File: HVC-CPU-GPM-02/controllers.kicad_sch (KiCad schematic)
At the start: 40 parts, among them P2 EXPANSION, P4 CONTROLLER 1, P5 CONTROLLER 2, U7 74LS368, U8 74LS368

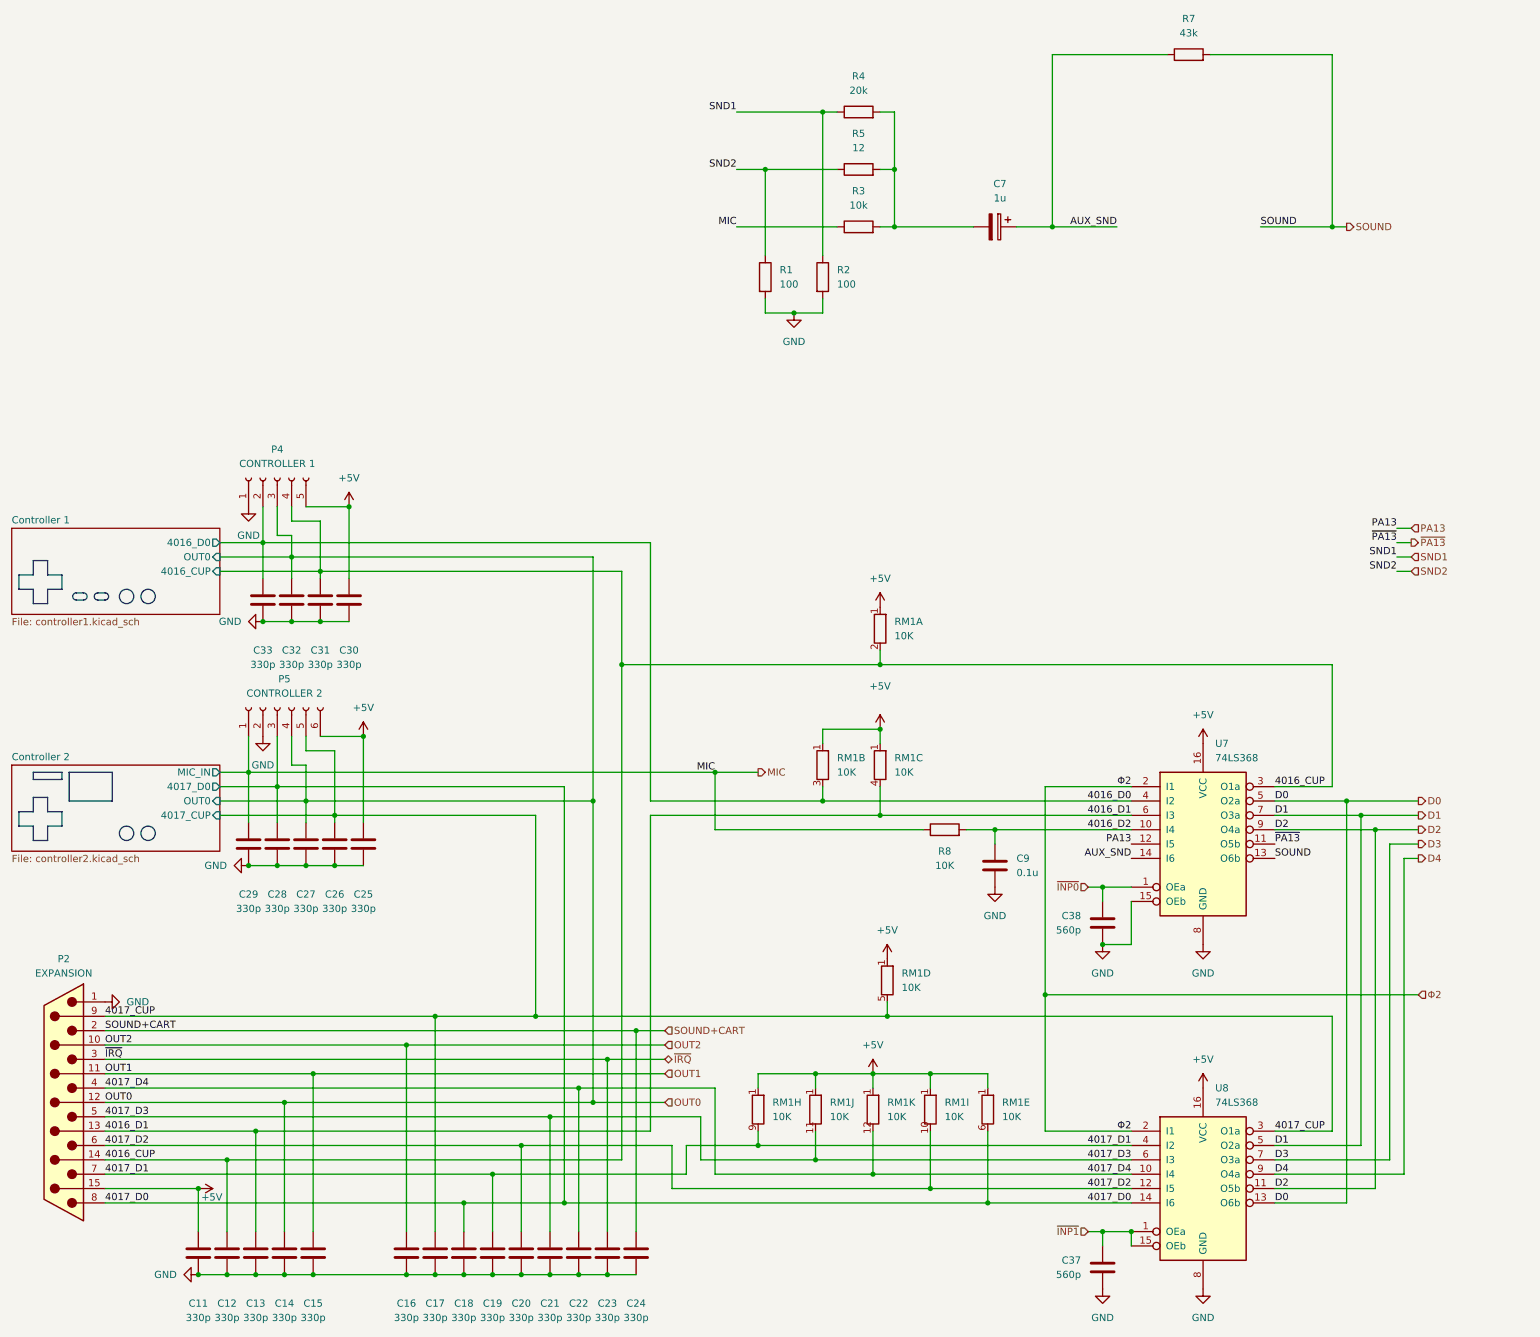
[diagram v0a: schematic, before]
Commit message: Refactor schematic: * Move audio and video circuits to dedicated sheet * Move power and mechanical to dedicated sheet Modify P1 Cart Connector symbol to: * split out audio ports * organize pins for easier wiring Modify 74LS346 symbol: * Split A/B ports to allow moving functions to related circuits Modify X1 crystal footprint: * change from stock footprint to custom footprint Correct crystal name from Y1 to X1
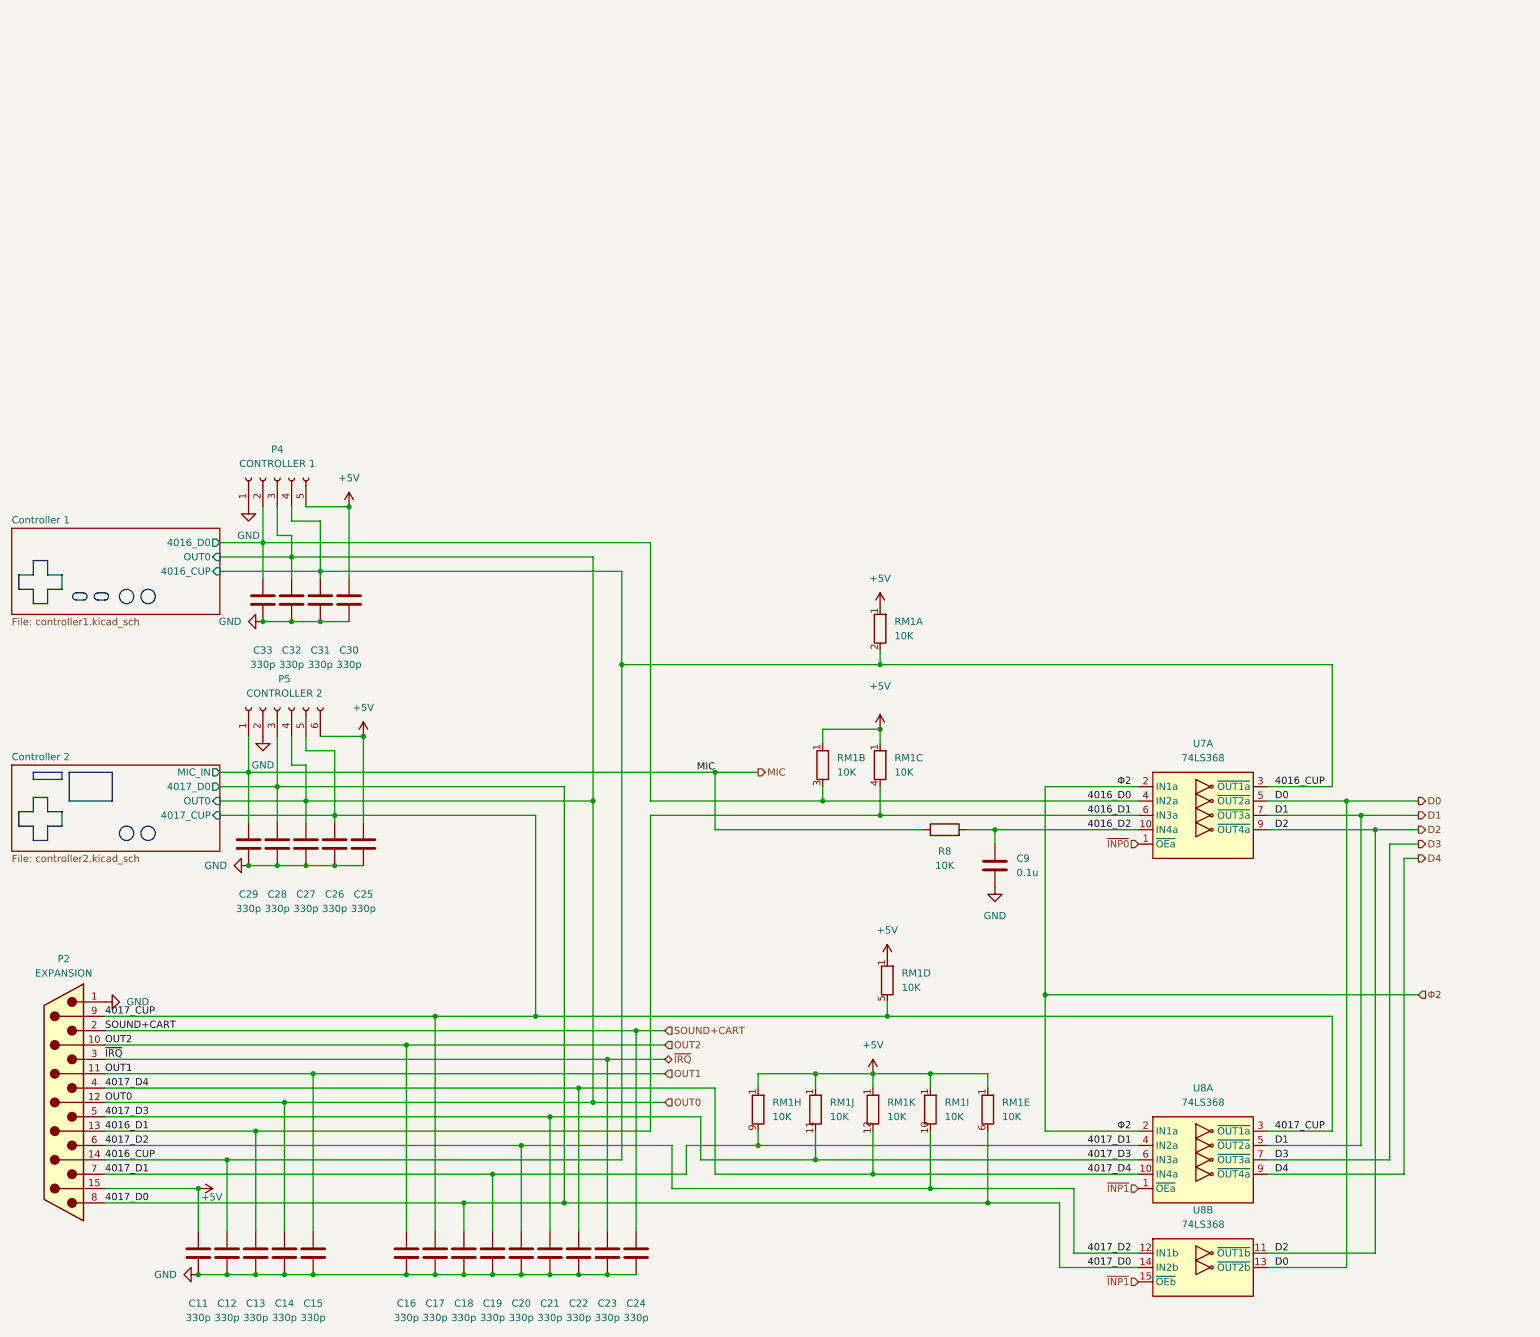
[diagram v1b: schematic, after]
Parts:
- removed C37, C38: 560p, Nintendo:C_Disc_D3.0mm_W2.0mm_P3.0mm, symbol Device:C
- removed C7: 1u, Capacitor_THT:CP_Radial_D5.0mm_P2.50mm, symbol Device:C_Polarized
- removed R1, R2: 100, Resistor_THT:R_Axial_DIN0207_L6.3mm_D2.5mm_P10.16mm_Horizontal, symbol Device:R
- removed R3: 10k, Resistor_THT:R_Axial_DIN0207_L6.3mm_D2.5mm_P10.16mm_Horizontal, symbol Device:R
- removed R4: 20k, Resistor_THT:R_Axial_DIN0207_L6.3mm_D2.5mm_P10.16mm_Horizontal, symbol Device:R
- removed R5: 12, Resistor_THT:R_Axial_DIN0207_L6.3mm_D2.5mm_P10.16mm_Horizontal, symbol Device:R
- removed R7: 43k, Resistor_THT:R_Axial_DIN0207_L6.3mm_D2.5mm_P10.16mm_Horizontal, symbol Device:R
- removed U8: 74LS368, Package_DIP:DIP-16_W7.62mm, symbol 74xx:74LS368
- added U8: 74LS368, Package_DIP:DIP-16_W7.62mm, symbol Famicom:74LS368
- U7: symbol 74xx:74LS368 -> Famicom:74LS368
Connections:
- net +5V: no longer U7.16 (VCC)
- net 4017_CUP: now also U8.3 (~{OUT1a})
- net 4017_D0: now also U8.14 (IN2b)
- net 4017_D1: now also U8.4 (IN2a)
- net 4017_D2: now also U8.12 (IN1b)
- net 4017_D3: now also U8.6 (IN3a)
- net 4017_D4: now also U8.10 (IN4a)
- net D0: now also U8.13 (~{OUT2b})
- net D1: now also U8.5 (~{OUT2a})
- net D2: now also U8.11 (~{OUT1b})
- net D3: now also U8.7 (~{OUT3a})
- net D4: now also U8.9 (~{OUT4a})
- net GND: no longer U7.15 (OEb), U7.8 (GND)
- net ~{INP1}: now also U8.1 (~{OEa}), U8.15 (~{OEb})
- net Φ2: now also U8.2 (IN1a)
- removed net AUX_SND: U7.14 (I6)
- removed net PA13: U7.12 (I5)
- removed net SOUND: U7.13 (O6b)
- removed net ~{PA13}: U7.11 (O5b)

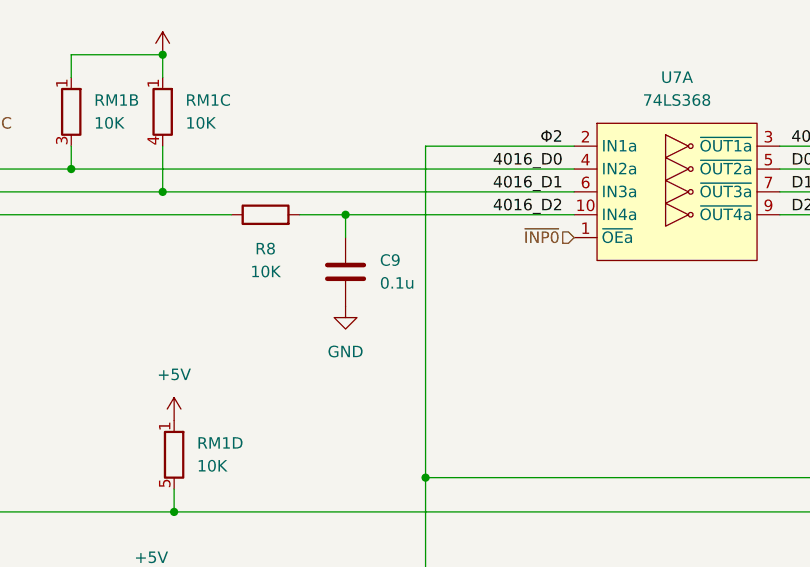
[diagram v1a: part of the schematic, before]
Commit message: Change symbols to functional layout instead of pin map layout Add technical page to store pinouts Organize and compact root page
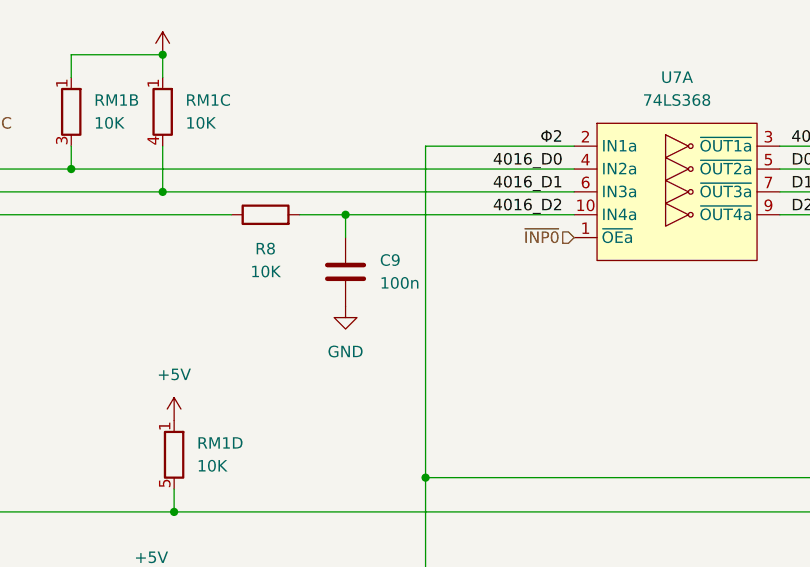
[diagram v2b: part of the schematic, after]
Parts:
- C9: value 0.1u -> 100n
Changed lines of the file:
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@@
 			)
 		)
-		(property "Value" "0.1u"
+		(property "Value" "100n"
 			(at 194.31 88.8999 0)
 			(effects

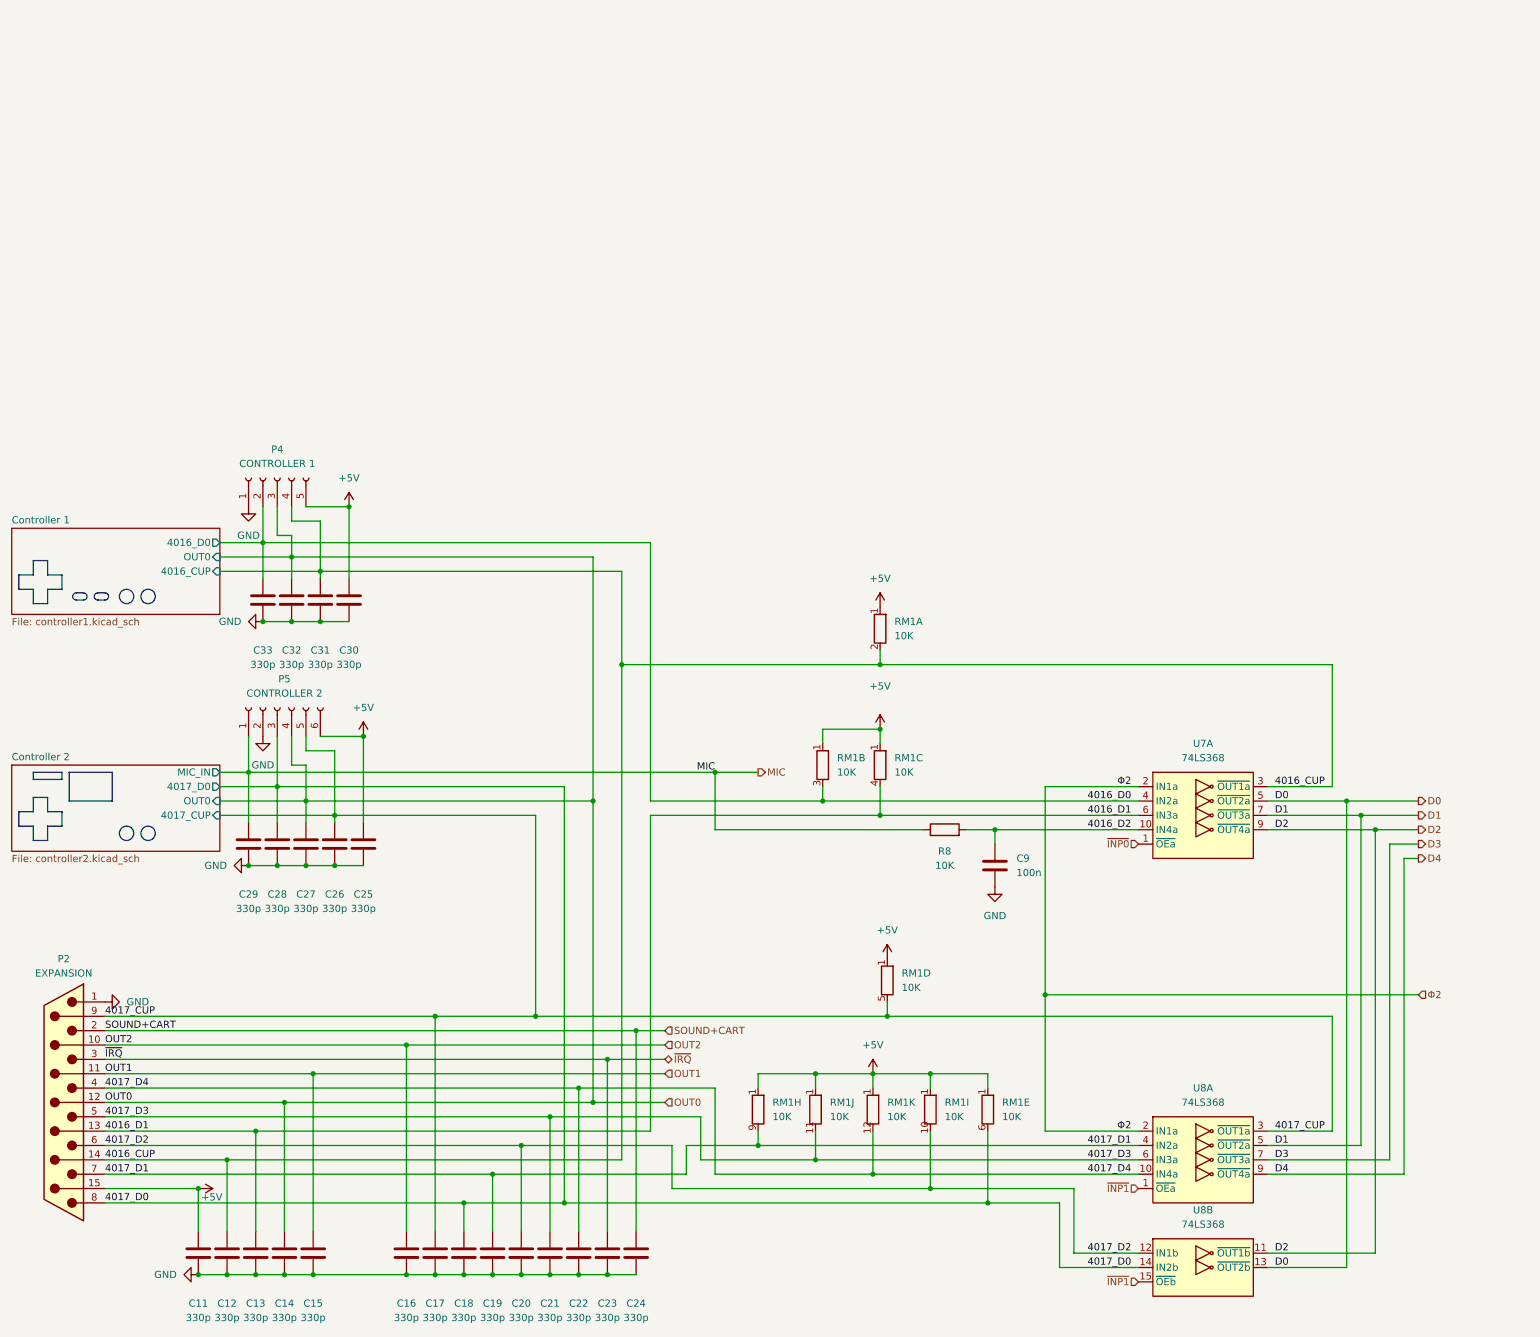
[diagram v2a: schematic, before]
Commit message: Rearranged pins on some symbols to simplify schematic wiring Removed schematics for controller PCBs Added PNG version of schematics
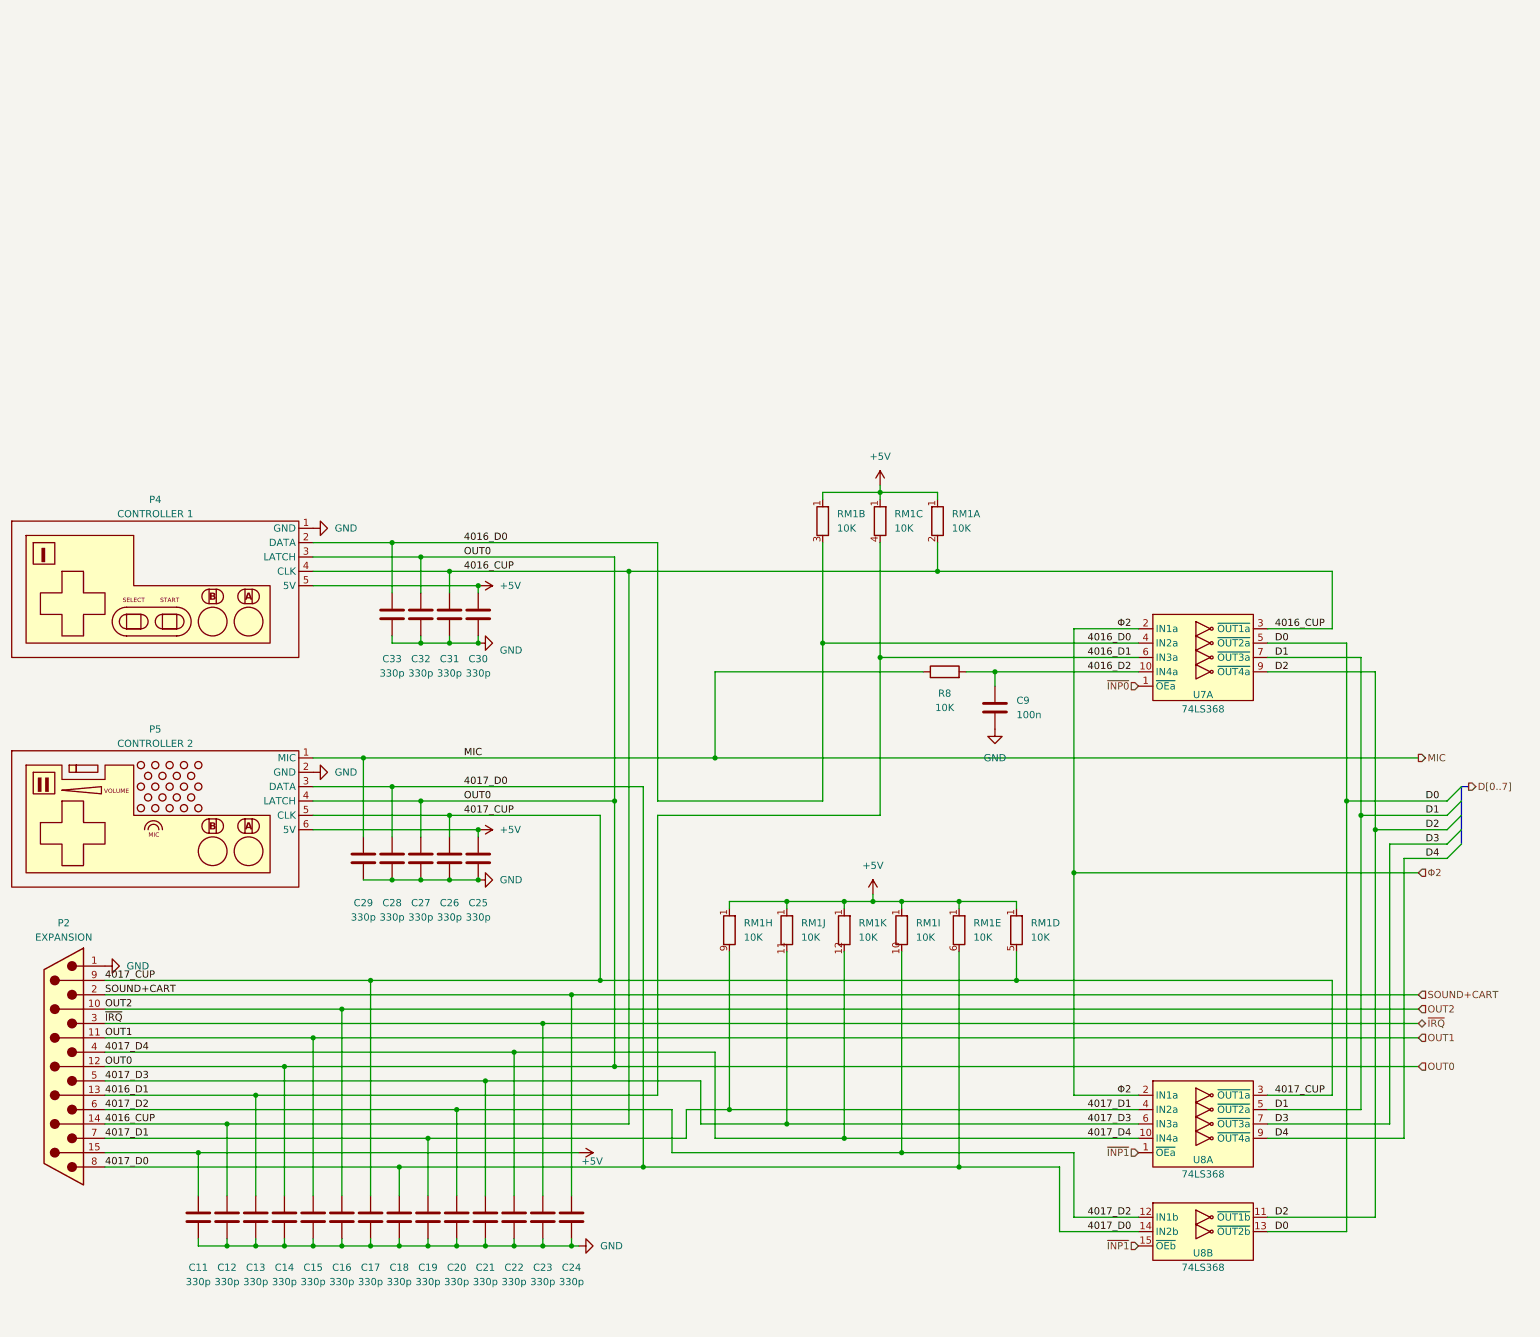
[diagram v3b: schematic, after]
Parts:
- removed P4: CONTROLLER 1, Nintendo:connector_2mm_5pin, symbol Connector:Conn_01x05_Socket
- removed P5: CONTROLLER 2, Nintendo:connector_2mm_6pin, symbol Connector:Conn_01x06_Socket
- added P4: CONTROLLER 1, Nintendo:connector_2mm_5pin, symbol Famicom:CONTROLLER1
- added P5: CONTROLLER 2, Nintendo:connector_2mm_6pin, symbol Famicom:CONTROLLER2
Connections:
- net +5V: now also P4.5 (5V), P5.6 (5V)
- net 4016_CUP: now also P4.4 (CLK)
- net 4016_D0: now also P4.2 (DATA)
- net 4017_CUP: now also P5.5 (CLK)
- net 4017_D0: now also P5.3 (DATA)
- net GND: now also P4.1 (GND), P5.2 (GND)
- net MIC: now also P5.1 (MIC)
- net OUT0: now also P4.3 (LATCH), P5.4 (LATCH)
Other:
- removed sheet Controller 1
- removed sheet Controller 2
- title: (none) -> Nintendo Famicom Mainboard
- moved on the sheet: C11, C12, C13, C14, C15, C16, C17, C18, C19, C20, C21, C22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
